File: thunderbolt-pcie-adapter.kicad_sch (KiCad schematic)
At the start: 8 parts

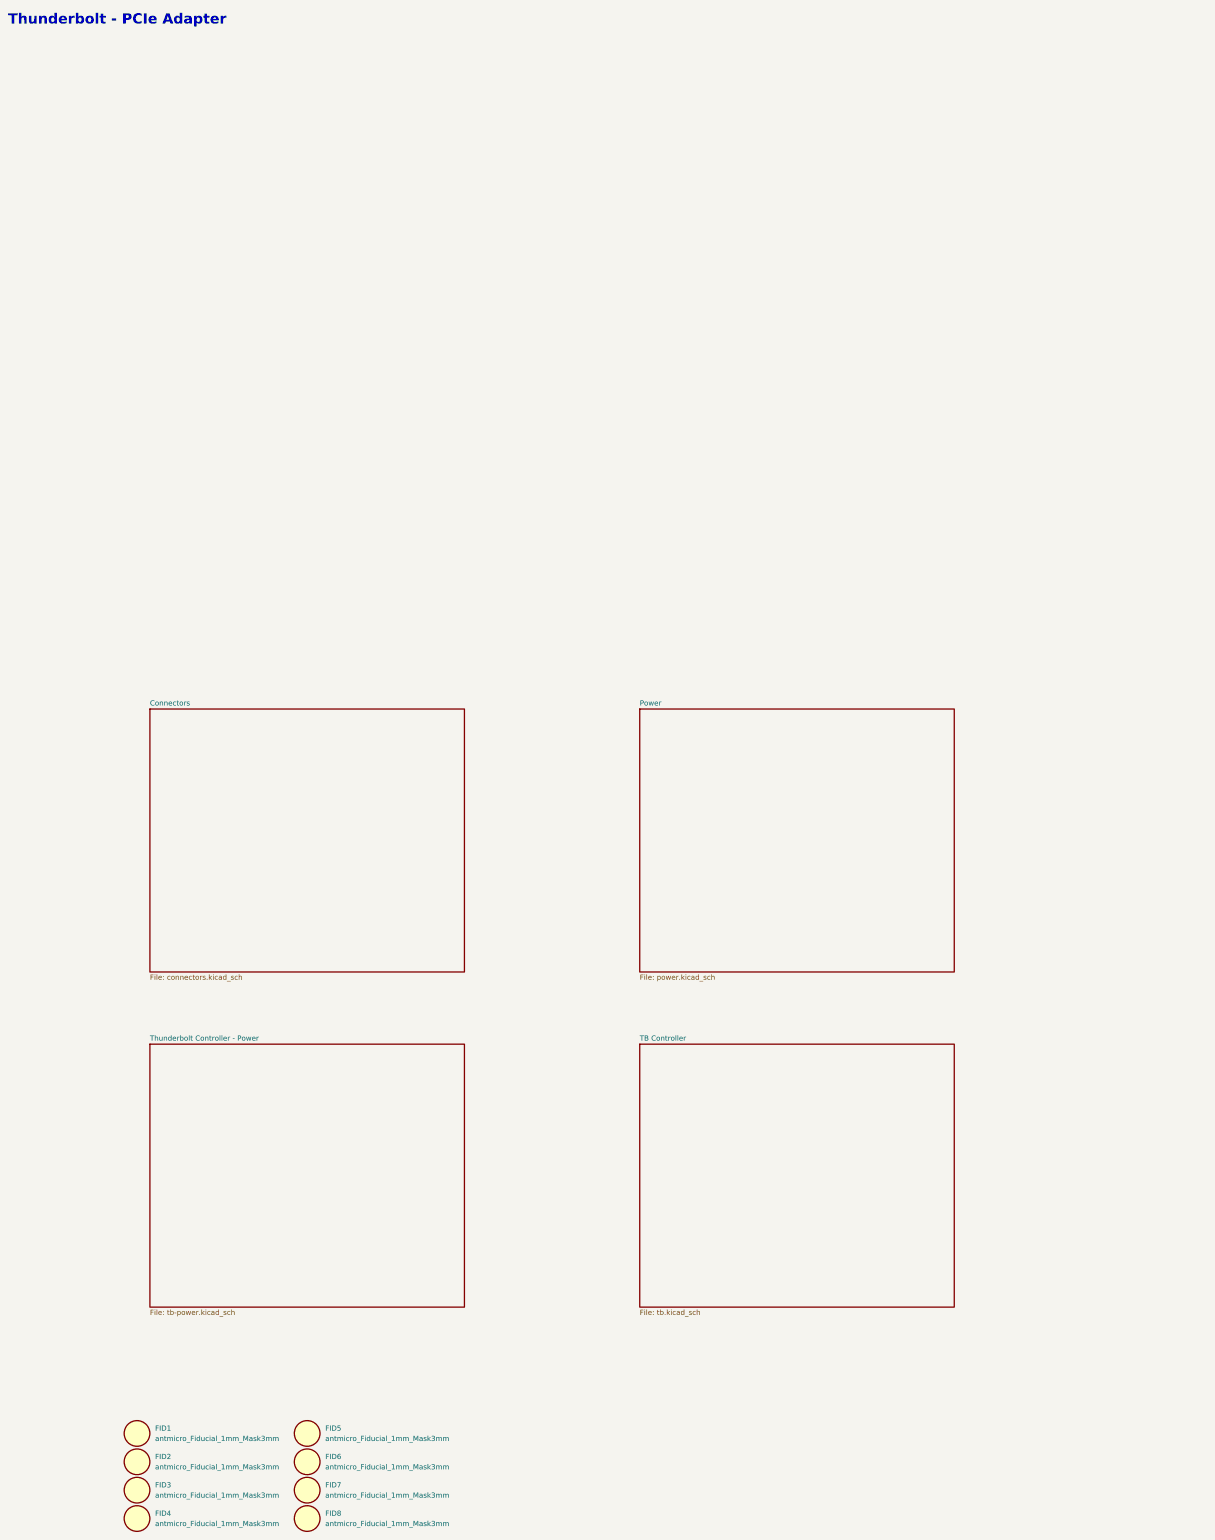
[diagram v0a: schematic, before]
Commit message: Change symbol of U4, redraw schematic to use landscape orientation
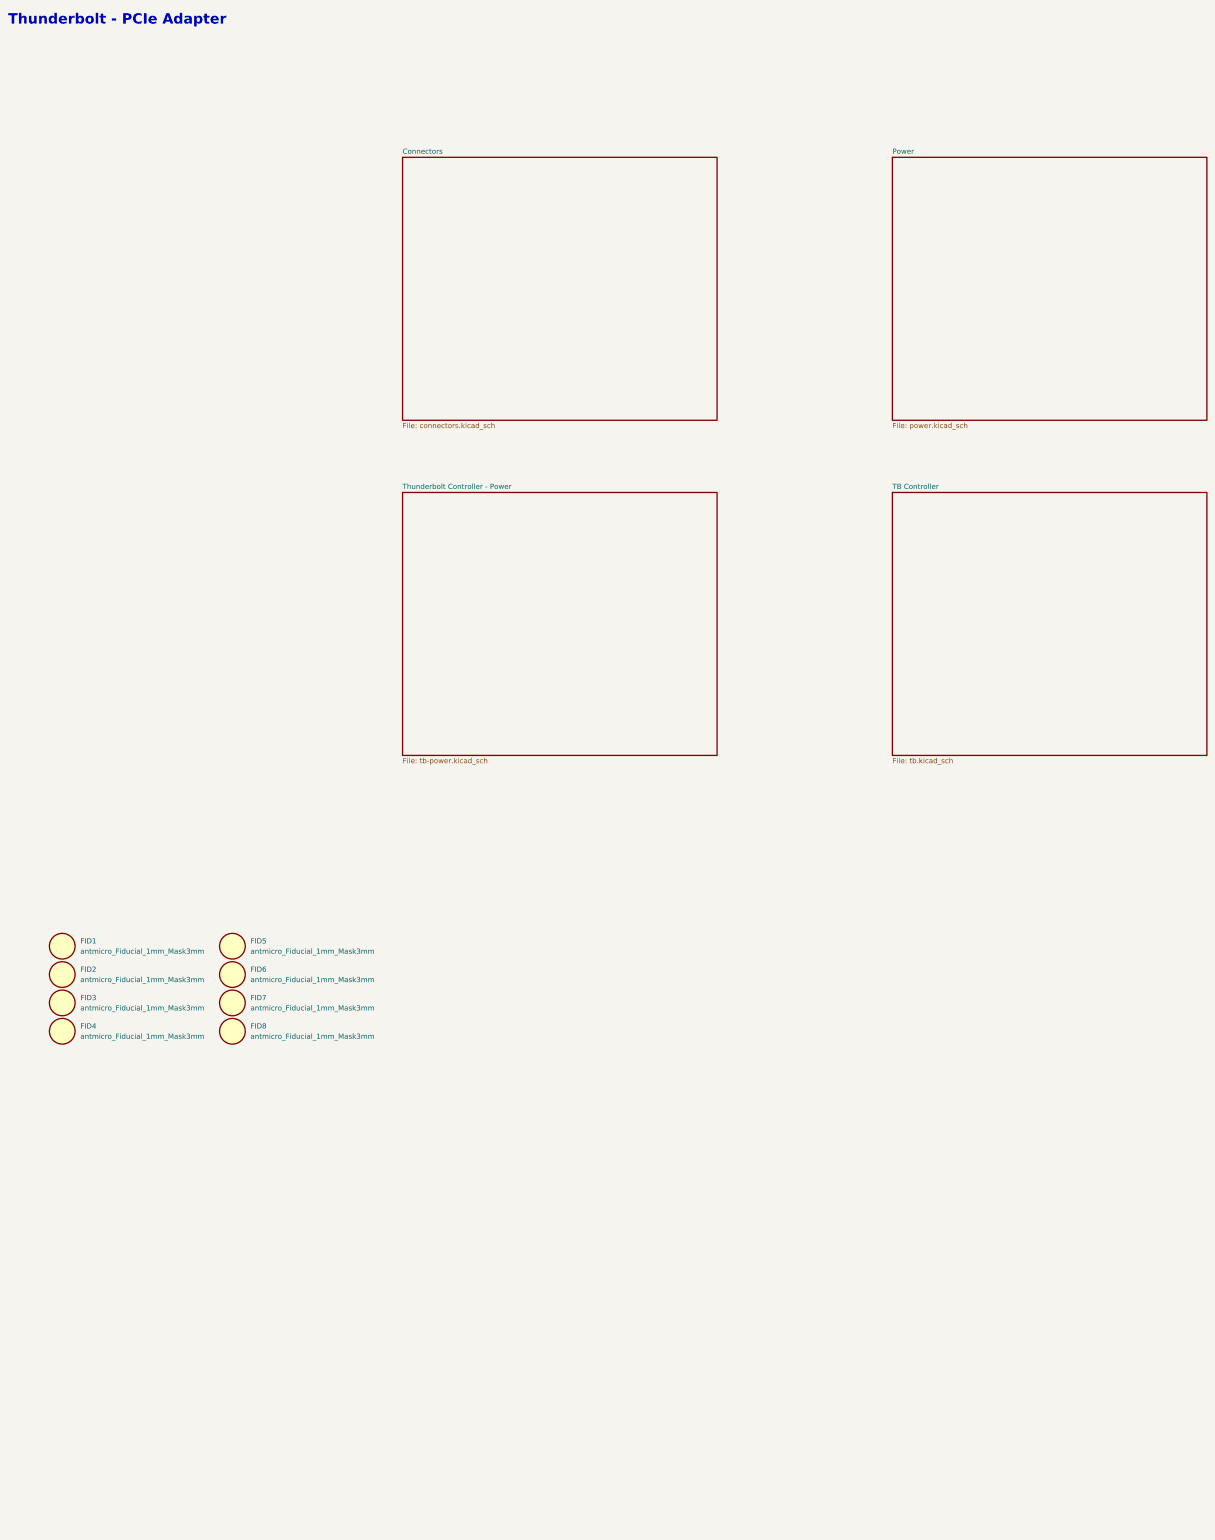
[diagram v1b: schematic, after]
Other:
- moved on the sheet: FID1, FID2, FID3, FID4, FID5, FID6, FID7, FID8

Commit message: Generate library of local components
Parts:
- FID1, FID2, FID3, FID4, FID5, FID6, FID7, FID8: footprint antmicro-footprints:Fiducial_1mm_Mask3mm -> thunderbolt-pcie-adapter-footprints:Fiducial_1mm_Mask3mm; symbol antmicroFiducialMarks:antmicro_Fiducial_1mm_Mask3mm -> thunderbolt-pcie-adapter:antmicro_Fiducial_1mm_Mask3mm
